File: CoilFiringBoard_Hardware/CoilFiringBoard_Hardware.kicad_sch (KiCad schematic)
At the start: 0 parts

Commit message: Made schematic
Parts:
- added Conn1: Molex_SL_02, symbol MRDT_Connectors:Molex_SL_02
- added D1: D, symbol Device:D
- added J1: Screw_Terminal_01x06, symbol Connector:Screw_Terminal_01x06
- added L1: L, symbol Device:L
- added Q1: NMOS, symbol Simulation_SPICE:NMOS
- added Q2, Q3, Q4: PMOS, symbol Simulation_SPICE:PMOS
- added R1, R2: 10k, symbol Device:R
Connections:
- new net: Q1.1 (D), R2.2
- new net: Conn1.2, Q1.2 (G)
- new net: D1.1 (K), L1.1, Q2.1 (D), Q3.1 (D), Q4.1 (D)
- new net: J1.4 (Pin_4), J1.5 (Pin_5), J1.6 (Pin_6), Q2.3 (S), Q3.3 (S), Q4.3 (S), R1.1
- new net GND: D1.2 (A), J1.1 (Pin_1), J1.2 (Pin_2), J1.3 (Pin_3), L1.2, Q1.3 (S)
- new net V_div: Q2.2 (G), Q3.2 (G), Q4.2 (G), R1.2, R2.1
- no-connect marks 0 -> 1
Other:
- note added: "<- to Cap Bank PWR"
- note added: "<- to Control Board Fire Signal"
- note added: "Coil"
- note added: "Connectors"
- note added: "GND"
- note added: "Logic"
- note added: "PWR"
- note added: "PWR FETs"
- note removed: "Cap bank connector Power MOSFET Coil"
- note removed: "Control board connector optical sensor"

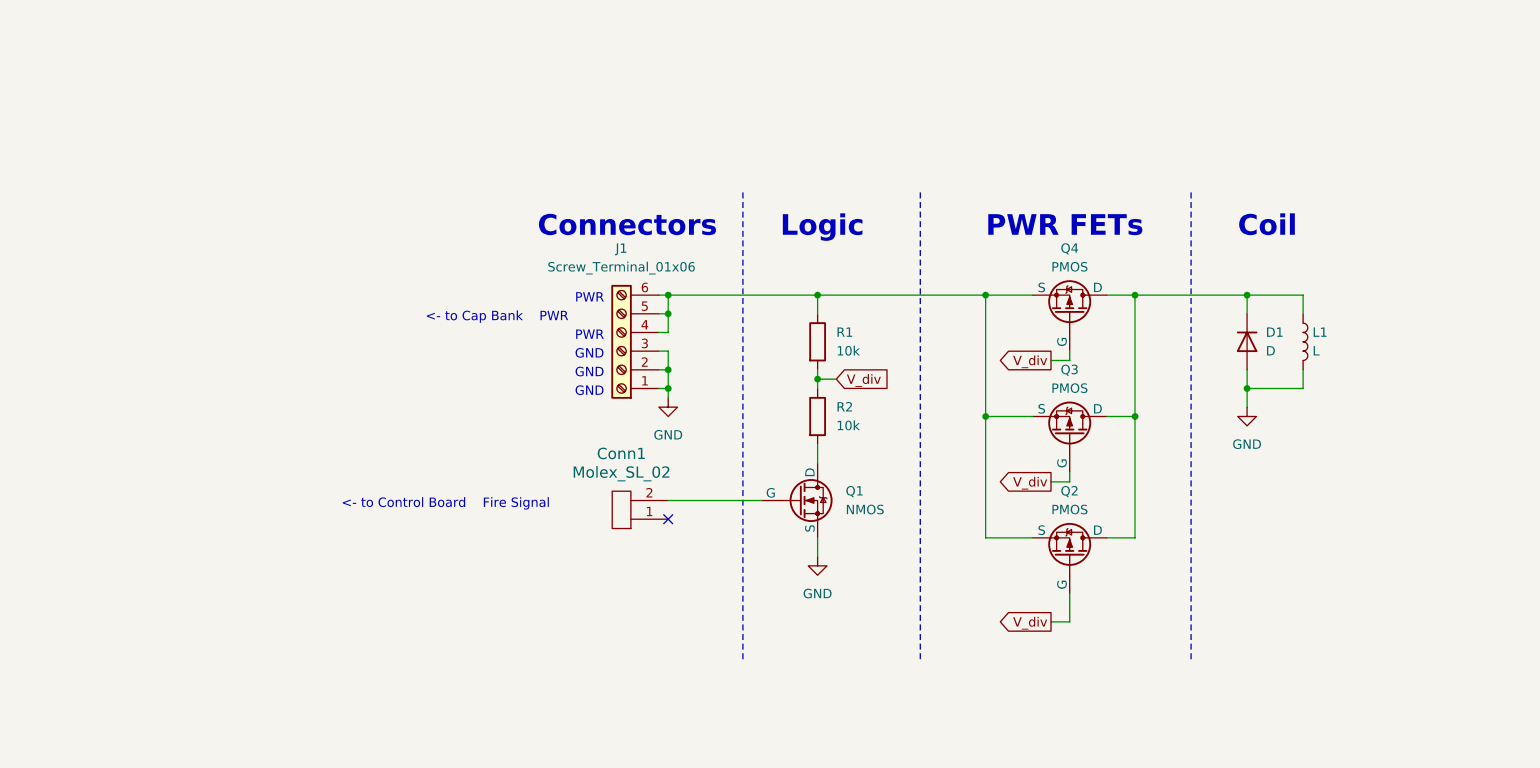
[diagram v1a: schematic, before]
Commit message: Changed FETs + added flyback diodes
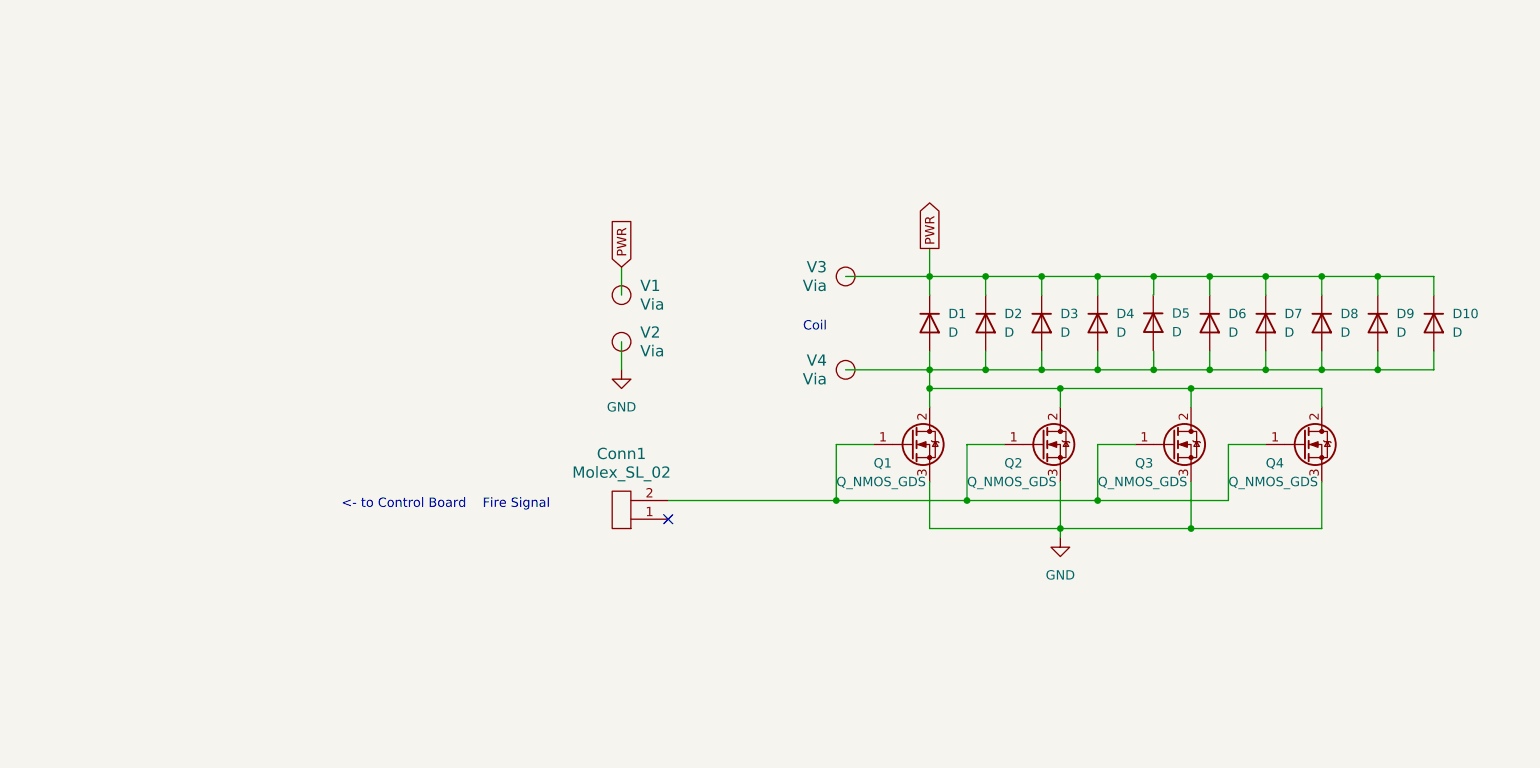
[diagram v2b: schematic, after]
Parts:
- removed J1: Screw_Terminal_01x06, symbol Connector:Screw_Terminal_01x06
- removed L1: L, symbol Device:L
- removed Q1: NMOS, symbol Simulation_SPICE:NMOS
- removed Q2, Q3, Q4: PMOS, symbol Simulation_SPICE:PMOS
- removed R1, R2: 10k, symbol Device:R
- added D10, D2, D3, D4, D5, D6, D7, D8, D9: D, Diode_THT:D_DO-15_P12.70mm_Horizontal, symbol Device:D
- added Q1, Q2, Q3, Q4: Q_NMOS_GDS, Package_TO_SOT_THT:TO-264-3_Vertical, symbol Device:Q_NMOS_GDS
- added V1, V2, V3, V4: Via, MRDT_Drill_Holes:BATT_PWR_VIA, symbol MRDT_Drill_Holes:Via
- Conn1: footprint (none) -> MRDT_Connectors:MOLEX_SL_02_Horizontal
- D1: footprint (none) -> Diode_THT:D_DO-15_P12.70mm_Horizontal
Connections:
- net GND: now also Q1.3 (S), Q2.3 (S), Q3.3 (S), Q4.3 (S), V2.1; no longer D1.2 (A)
- net at Conn1.2: now also Q1.1 (G), Q2.1 (G), Q3.1 (G), Q4.1 (G)
- net PWR: now reaches D1.1 (K)
- net PWR: now also D10.1 (K), D2.1 (K), D3.1 (K), D4.1 (K), D6.1 (K), D7.1 (K), D8.1 (K), D9.1 (K), V1.1, V3.1
- new net: D1.2 (A), D10.2 (A), D2.2 (A), D3.2 (A), D4.2 (A), D6.2 (A), D7.2 (A), D8.2 (A), D9.2 (A), Q1.2 (D), Q2.2 (D), Q3.2 (D), Q4.2 (D), V4.1
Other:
- note removed: "<- to Cap Bank PWR"
- note removed: "Connectors"
- note removed: "GND"
- note removed: "Logic"
- note removed: "PWR"
- note removed: "PWR FETs"

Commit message: Made layout
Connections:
- net PWR: now also D5.1 (K)
- net Coil-: now reaches D1.2 (A), D10.2 (A), D2.2 (A), D3.2 (A), D4.2 (A), D6.2 (A), D7.2 (A), D8.2 (A), D9.2 (A), Q1.2 (D), Q2.2 (D), Q3.2 (D), Q4.2 (D), V4.1
- net Coil-: now also D5.2 (A)
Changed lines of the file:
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@@
   (junction (at 168.91 73.66) (diameter 0) (color 0 0 0 0)
+  )
+  (junction (at 214.63 73.66) (diameter 0) (color 0 0 0 0)
   )
   (junction (at 151.13 91.44) (diameter 0) (color 0 0 0 0)
@@
   )
   (wire (pts (xy 207.01 60.96) (xy 207.01 63.5))
+    (stroke (width 0) (type default))
+  )
+  (wire (pts (xy 214.63 73.66) (xy 217.17 73.66))
     (stroke (width 0) (type default))
   )
@@
     )
   )
+  (global_label "Coil-" (shape input) (at 217.17 73.66 0) (fields_autoplaced)
+    (effects (font (size 1.27 1.27)) (justify left))
+    (property "Intersheetrefs" "${INTERSHEET_REFS}" (at 225.3372 73.66 0)
+      (effects (font (size 1.27 1.27)) (justify left) hide)
+    )
+  )
   (global_label "PWR" (shape output) (at 146.05 57.15 90) (fields_autoplaced)
     (effects (font (size 1.27 1.27)) (justify left))
@@
     )
   )
-  (symbol (lib_id "Device:D") (at 176.4671 67.2504 270) (unit 1)
-    (in_bom yes) (on_board yes) (dnp no) (fields_autoplaced)
-    (property "Reference" "D5" (at 179.0071 65.9804 90)
-      (effects (font (size 1.27 1.27)) (justify left))
-    )
-    (property "Value" "D" (at 179.0071 68.5204 90)
-      (effects (font (size 1.27 1.27)) (justify left))
-    )
-    (property "Footprint" "Diode_THT:D_DO-15_P12.70mm_Horizontal" (at 176.4671 67.2504 0)
-      (effects (font (size 1.27 1.27)) hide)
-    )
-    (property "Datasheet" "https://goodarksemi.com/docs/datasheets/general_purpose_rectifiers/GSRxxx.pdf" (at 176.4671 67.2504 0)
-      (effects (font (size 1.27 1.27)) hide)
-    )
-    (property "Sim.Device" "D" (at 176.4671 67.2504 0)
-      (effects (font (size 1.27 1.27)) hide)
-    )
-    (property "Sim.Pins" "1=K 2=A" (at 176.4671 67.2504 0)
-      (effects (font (size 1.27 1.27)) hide)
-    )
+  (symbol (lib_id "Device:D") (at 176.53 67.31 270) (unit 1)
+    (in_bom yes) (on_board yes) (dnp no) (fields_autoplaced)
+    (property "Reference" "D5" (at 179.07 66.04 90)
+      (effects (font (size 1.27 1.27)) (justify left))
+    )
+    (property "Value" "D" (at 179.07 68.58 90)
+      (effects (font (size 1.27 1.27)) (justify left))
+    )
+    (property "Footprint" "Diode_THT:D_DO-15_P12.70mm_Horizontal" (at 176.53 67.31 0)
+      (effects (font (size 1.27 1.27)) hide)
+    )
+    (property "Datasheet" "https://goodarksemi.com/docs/datasheets/general_purpose_rectifiers/GSRxxx.pdf" (at 176.53 67.31 0)
+      (effects (font (size 1.27 1.27)) hide)
+    )
+    (property "Sim.Device" "D" (at 176.53 67.31 0)
+      (effects (font (size 1.27 1.27)) hide)
+    )
+    (property "Sim.Pins" "1=K 2=A" (at 176.53 67.31 0)
+      (effects (font (size 1.27 1.27)) hide)
+    )

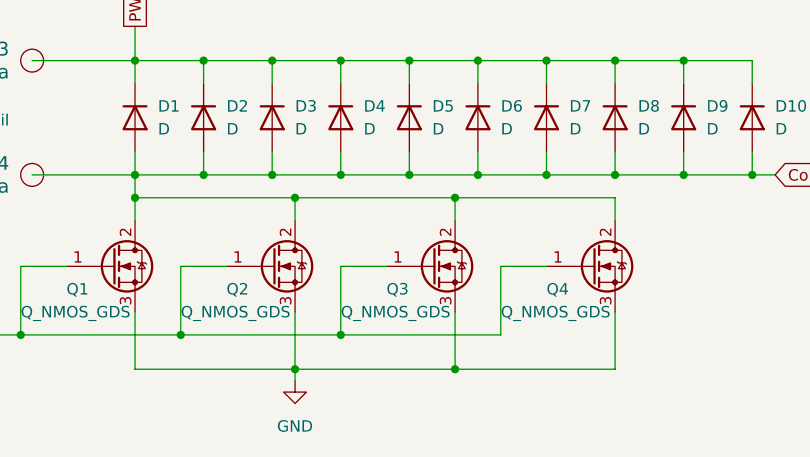
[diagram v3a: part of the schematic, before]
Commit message: Updated layout
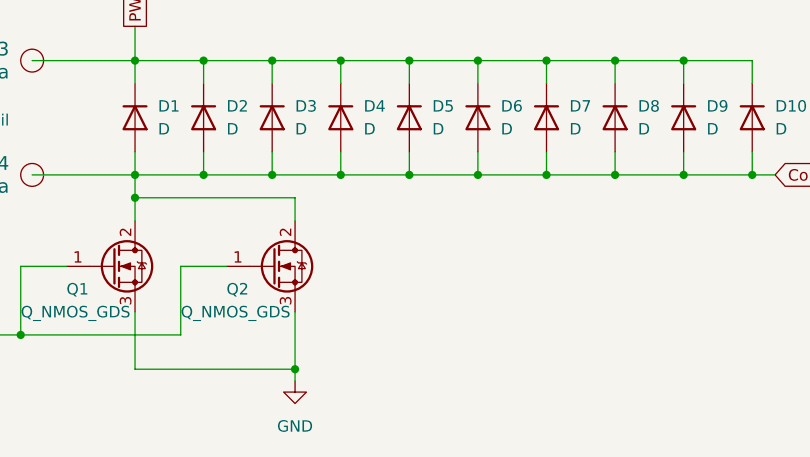
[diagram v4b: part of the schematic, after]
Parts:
- removed Q3, Q4: Q_NMOS_GDS, Package_TO_SOT_THT:TO-264-3_Vertical, symbol Device:Q_NMOS_GDS
- V3, V4: footprint MRDT_Drill_Holes:BATT_PWR_VIA -> MountingHole:MountingHole_2.2mm_M2_DIN965_Pad
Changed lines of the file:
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@@
   (junction (at 214.63 73.66) (diameter 0) (color 0 0 0 0)
   )
-  (junction (at 151.13 91.44) (diameter 0) (color 0 0 0 0)
-  )
   (junction (at 184.15 73.66) (diameter 0) (color 0 0 0 0)
   )
@@
   (junction (at 146.05 60.96) (diameter 0) (color 0 0 0 0)
   )
-  (junction (at 181.61 76.2) (diameter 0) (color 0 0 0 0)
-  )
   (junction (at 199.39 60.96) (diameter 0) (color 0 0 0 0)
   )
@@
   (junction (at 153.67 73.66) (diameter 0) (color 0 0 0 0)
   )
-  (junction (at 168.91 91.44) (diameter 0) (color 0 0 0 0)
-  )
   (junction (at 176.53 73.66) (diameter 0) (color 0 0 0 0)
   )
-  (junction (at 181.61 95.25) (diameter 0) (color 0 0 0 0)
-  )
   (junction (at 161.29 60.96) (diameter 0) (color 0 0 0 0)
   )
@@
   )
   (junction (at 184.15 60.96) (diameter 0) (color 0 0 0 0)
-  )
-  (junction (at 163.83 76.2) (diameter 0) (color 0 0 0 0)
   )
   (junction (at 207.01 73.66) (diameter 0) (color 0 0 0 0)
@@
     (stroke (width 0) (type default))
   )
-  (wire (pts (xy 181.61 88.9) (xy 181.61 95.25))
-    (stroke (width 0) (type default))
-  )
   (wire (pts (xy 146.05 73.66) (xy 146.05 76.2))
     (stroke (width 0) (type default))
   )
-  (wire (pts (xy 181.61 95.25) (xy 199.39 95.25))
-    (stroke (width 0) (type default))
-  )
   (wire (pts (xy 146.05 95.25) (xy 163.83 95.25))
     (stroke (width 0) (type default))
   )
-  (wire (pts (xy 181.61 76.2) (xy 181.61 78.74))
-    (stroke (width 0) (type default))
-  )
   (wire (pts (xy 199.39 60.96) (xy 207.01 60.96))
     (stroke (width 0) (type default))
@@
     (stroke (width 0) (type default))
   )
-  (wire (pts (xy 168.91 83.82) (xy 168.91 91.44))
-    (stroke (width 0) (type default))
-  )
-  (wire (pts (xy 199.39 88.9) (xy 199.39 95.25))
-    (stroke (width 0) (type default))
-  )
   (wire (pts (xy 161.29 71.12) (xy 161.29 73.66))
     (stroke (width 0) (type default))
@@
     (stroke (width 0) (type default))
   )
-  (wire (pts (xy 163.83 76.2) (xy 181.61 76.2))
-    (stroke (width 0) (type default))
-  )
   (wire (pts (xy 163.83 76.2) (xy 146.05 76.2))
     (stroke (width 0) (type default))
@@
     (stroke (width 0) (type default))
   )
-  (wire (pts (xy 173.99 83.82) (xy 168.91 83.82))
-    (stroke (width 0) (type default))
-  )
-  (wire (pts (xy 186.69 83.82) (xy 186.69 91.44))
-    (stroke (width 0) (type default))
-  )
   (wire (pts (xy 168.91 71.12) (xy 168.91 73.66))
     (stroke (width 0) (type default))
   )
-  (wire (pts (xy 181.61 76.2) (xy 199.39 76.2))
-    (stroke (width 0) (type default))
-  )
   (wire (pts (xy 191.77 60.96) (xy 191.77 63.5))
     (stroke (width 0) (type default))
@@
     (stroke (width 0) (type default))
   )
-  (wire (pts (xy 199.39 76.2) (xy 199.39 78.74))
-    (stroke (width 0) (type default))
-  )
   (wire (pts (xy 153.67 73.66) (xy 161.29 73.66))
     (stroke (width 0) (type default))
@@
     (stroke (width 0) (type default))
   )
-  (wire (pts (xy 163.83 95.25) (xy 181.61 95.25))
-    (stroke (width 0) (type default))
-  )
-  (wire (pts (xy 186.69 91.44) (xy 168.91 91.44))
-    (stroke (width 0) (type default))
-  )
   (wire (pts (xy 191.77 73.66) (xy 199.39 73.66))
     (stroke (width 0) (type default))
@@
   )
   (wire (pts (xy 214.63 60.96) (xy 214.63 63.5))
-    (stroke (width 0) (type default))
-  )
-  (wire (pts (xy 168.91 91.44) (xy 151.13 91.44))
-    (stroke (width 0) (type default))
-  )
-  (wire (pts (xy 191.77 83.82) (xy 186.69 83.82))
     (stroke (width 0) (type default))
   )
@@
     )
   )
-  (symbol (lib_id "Device:Q_NMOS_GDS") (at 196.85 83.82 0) (unit 1)
-    (in_bom yes) (on_board yes) (dnp no)
-    (property "Reference" "Q4" (at 191.77 86.36 0)
-      (effects (font (size 1.27 1.27)) (justify left))
-    )
-    (property "Value" "Q_NMOS_GDS" (at 186.69 88.9 0)
-      (effects (font (size 1.27 1.27)) (justify left))
-    )
-    (property "Footprint" "Package_TO_SOT_THT:TO-264-3_Vertical" (at 201.93 81.28 0)
-      (effects (font (size 1.27 1.27)) hide)
-    )
-    (property "Datasheet" "https://www.onsemi.com/pdf/datasheet/fdl100n50f-d.pdf" (at 196.85 83.82 0)
-      (effects (font (size 1.27 1.27)) hide)
-    )
-    (pin "1")
-    (pin "2")
-    (pin "3")
-    (instances
-      (project "CoilFiringBoard_Hardware"
-        (path "/28c13569-1eb8-4279-9ec4-13288f6f9832"
-          (reference "Q4") (unit 1)
-        )
-      )
-    )
-  )
   (symbol (lib_id "MRDT_Drill_Holes:Via") (at 104.14 69.85 0) (unit 1)
     (in_bom yes) (on_board yes) (dnp no) (fields_autoplaced)
@@
       (effects (font (size 1.524 1.524)) (justify left))
     )
-    (property "Footprint" "MRDT_Drill_Holes:BATT_PWR_VIA" (at 134.62 73.66 0)
+    (property "Footprint" "MountingHole:MountingHole_2.2mm_M2_DIN965_Pad" (at 134.62 73.66 0)
       (effects (font (size 1.524 1.524)) hide)
     )
@@
       (effects (font (size 1.524 1.524)) (justify left))
     )
-    (property "Footprint" "MRDT_Drill_Holes:BATT_PWR_VIA" (at 134.62 60.96 0)
+    (property "Footprint" "MountingHole:MountingHole_2.2mm_M2_DIN965_Pad" (at 134.62 60.96 0)
       (effects (font (size 1.524 1.524)) hide)
     )
@@
         )
       )
-    )
-  )
-  (symbol (lib_id "Device:Q_NMOS_GDS") (at 179.07 83.82 0) (unit 1)
-    (in_bom yes) (on_board yes) (dnp no)
-    (property "Reference" "Q3" (at 173.99 86.36 0)
-      (effects (font (size 1.27 1.27)) (justify left))
-    )
-    (property "Value" "Q_NMOS_GDS" (at 168.91 88.9 0)
-      (effects (font (size 1.27 1.27)) (justify left))
-    )
-    (property "Footprint" "Package_TO_SOT_THT:TO-264-3_Vertical" (at 184.15 81.28 0)
-      (effects (font (size 1.27 1.27)) hide)
-    )
-    (property "Datasheet" "https://www.onsemi.com/pdf/datasheet/fdl100n50f-d.pdf" (at 179.07 83.82 0)
-      (effects (font (size 1.27 1.27)) hide)
-    )
-    (pin "1")
-    (pin "2")
-    (pin "3")
-    (instances
-      (project "CoilFiringBoard_Hardware"
-        (path "/28c13569-1eb8-4279-9ec4-13288f6f9832"
-          (reference "Q3") (unit 1)
-        )
-      )

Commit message: Updated layout
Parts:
- Conn1: footprint MRDT_Connectors:MOLEX_SL_02_Horizontal -> MRDT_Connectors:MOLEX_SL_02_Vertical
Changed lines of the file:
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@@
       (effects (font (size 1.524 1.524)))
     )
-    (property "Footprint" "MRDT_Connectors:MOLEX_SL_02_Horizontal" (at 105.41 87.63 0)
+    (property "Footprint" "MRDT_Connectors:MOLEX_SL_02_Vertical" (at 105.41 87.63 0)
       (effects (font (size 1.524 1.524)) hide)
     )

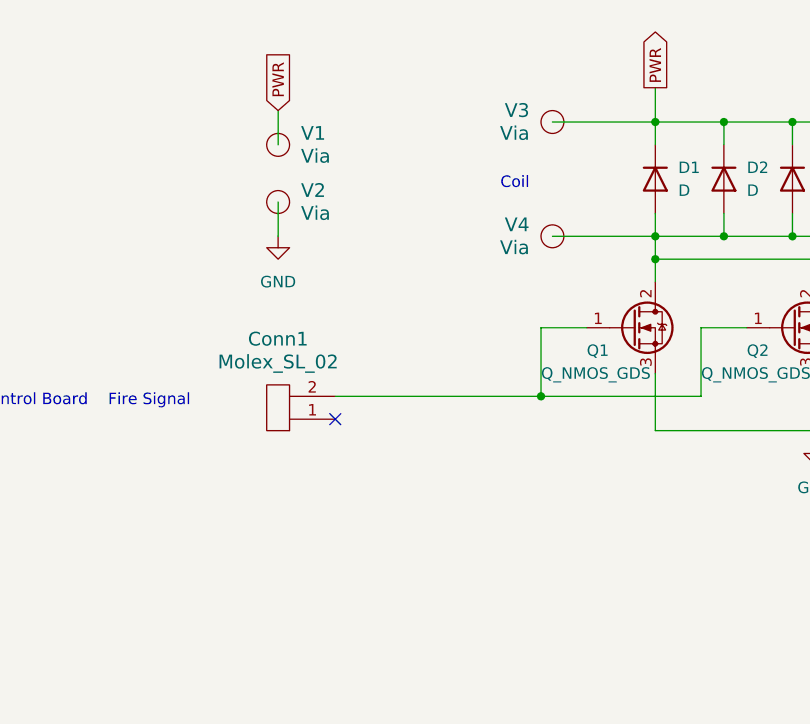
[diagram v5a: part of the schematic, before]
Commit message: Increased spacing + added Y cap
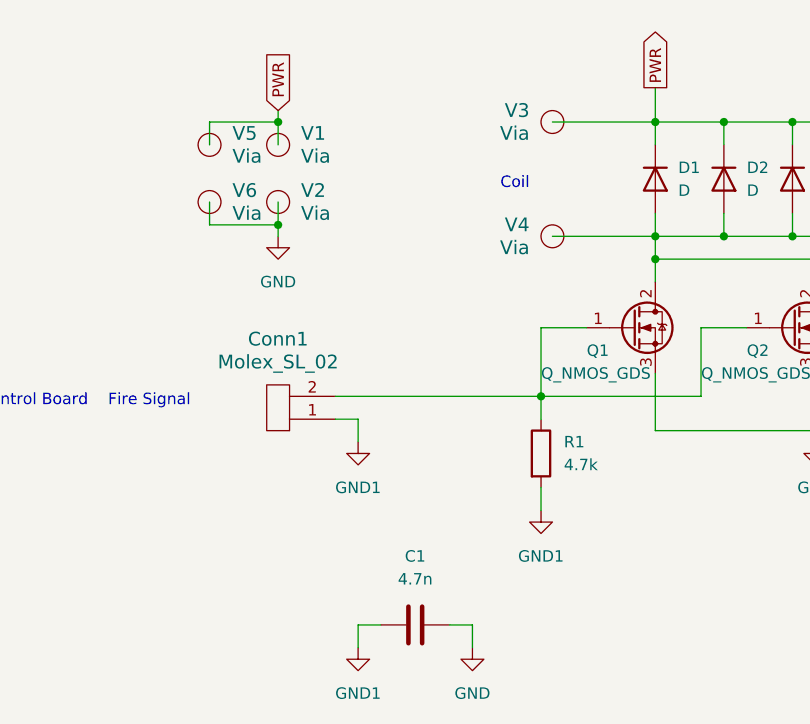
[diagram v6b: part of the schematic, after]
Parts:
- added C1: 4.7n, Capacitor_THT:CP_Radial_D10.0mm_P5.00mm, symbol Device:C
- added R1: 4.7k, Resistor_SMD:R_0603_1608Metric_Pad0.98x0.95mm_HandSolder, symbol Device:R
- added V5, V6: Via, MRDT_Drill_Holes:BATT_PWR_VIA, symbol MRDT_Drill_Holes:Via
- Conn1: footprint MRDT_Connectors:MOLEX_SL_02_Vertical -> MRDT_Connectors:MOLEX_SL_02_Horizontal
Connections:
- net GND: now also C1.2, V6.1
- net PWR: now also V5.1
- net at Conn1.2, Q1.1 (G), Q2.1 (G): now also R1.1
- net GND1: now reaches Conn1.1
- net GND1: now also C1.1, R1.2
- no-connect marks 1 -> 0
